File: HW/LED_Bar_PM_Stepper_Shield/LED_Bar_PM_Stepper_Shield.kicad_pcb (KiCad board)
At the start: 2 copper layers, 165.1 x 55.9 mm, 24 parts, among them J1 JST XH 5pin male socket, J2 JST XH 5pin male socket, J3 JST XH 5pin male socket, J4 JST XH 5pin male socket, J5 1x6 2.54mm female, pin2 filled, J6 1x6 2.54mm female, pin2 filled, J7 Extension of Ard Nano, filled, J8 Extension of Ard Nano, filled, U1 ULN2803A, U2 ULN2803A

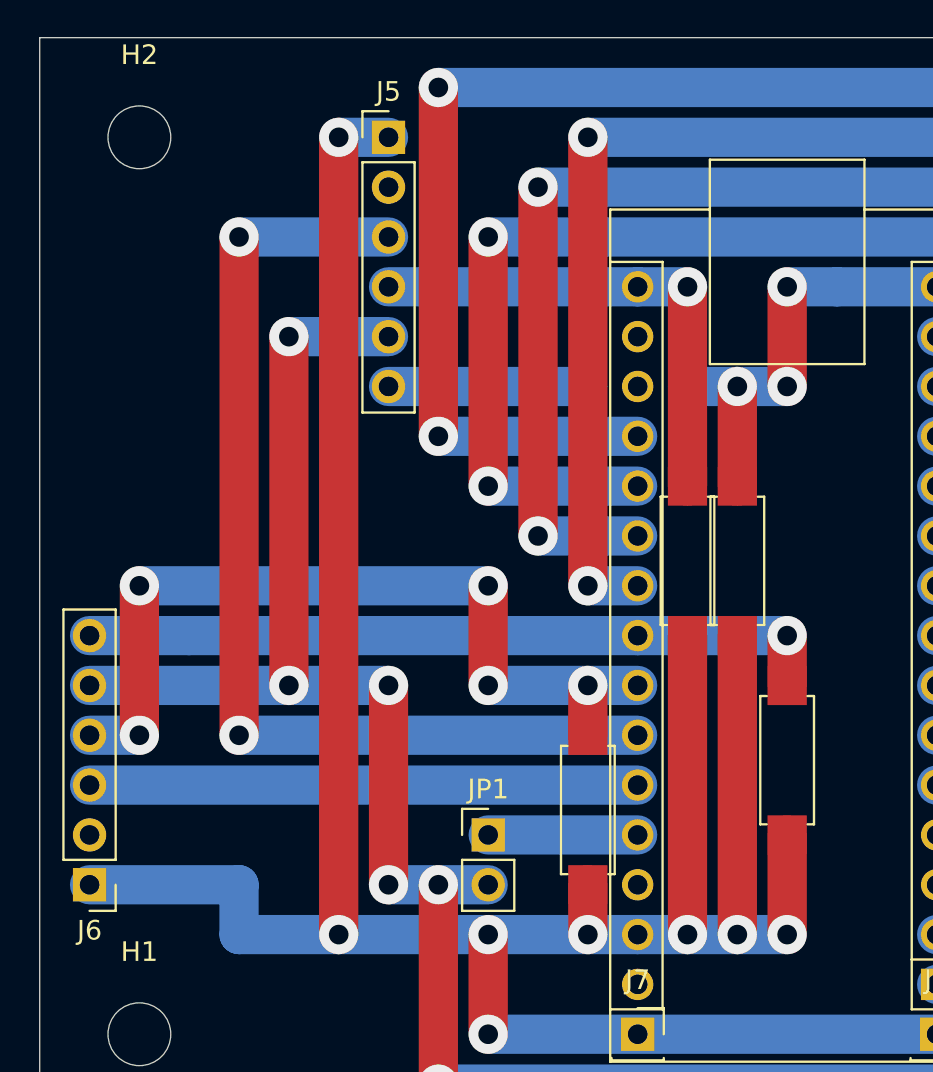
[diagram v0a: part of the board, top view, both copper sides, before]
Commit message: Swapped GND and 5V so I can use internal Pull-up.
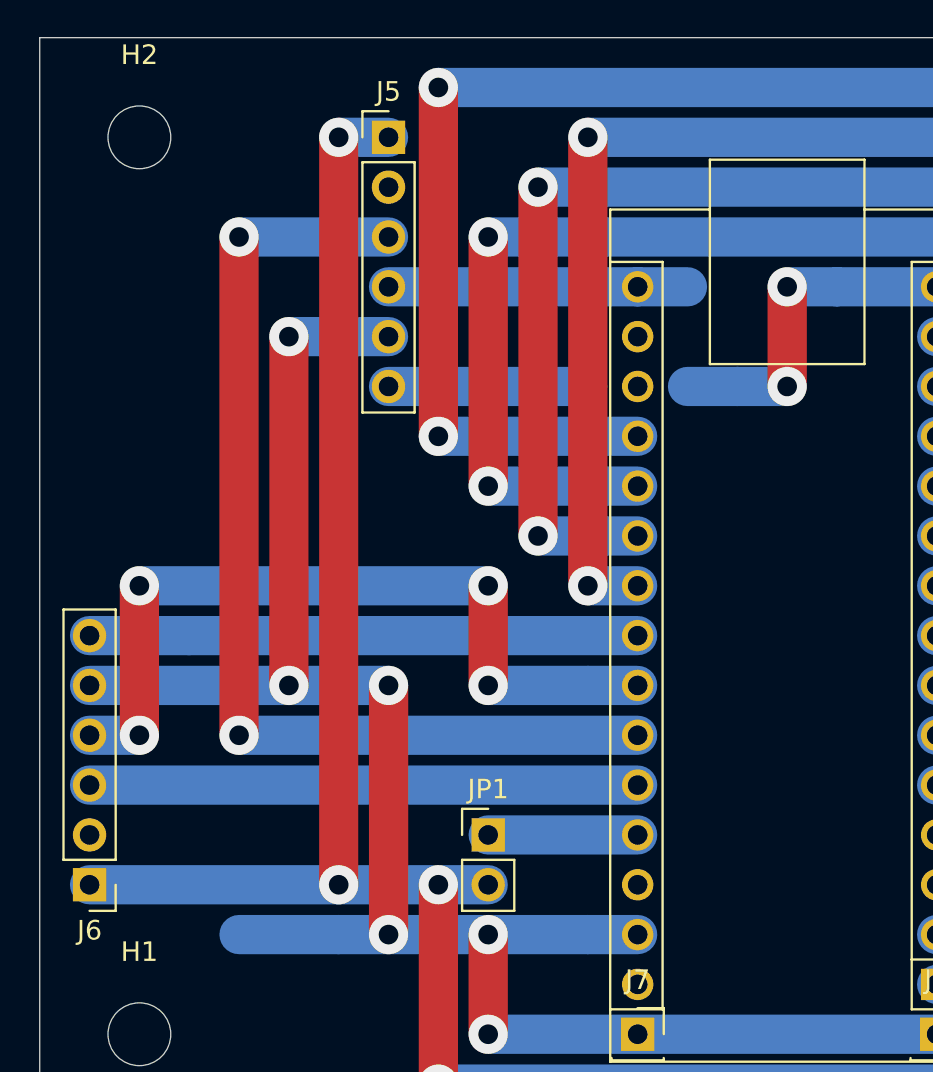
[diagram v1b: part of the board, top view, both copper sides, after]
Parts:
- removed R1, R2, R3, R4: 10k, For_Rasterboard:R_Axial_DIN0207_L6.3mm_D2.5mm_Pinf_Horizontal
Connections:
- J5 pad 1: GND -> +5V
- J5 pad 5: +5V -> GND
- J6 pad 1: GND -> +5V
- J6 pad 5: +5V -> GND
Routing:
- net GND: track 246.4 -> 198.1 mm, vias 12 -> 10
- net /DB1: track 38.1 -> 27.9 mm, vias 1 -> 0
- net /DA0: track 25.4 -> 15.2 mm, vias 1 -> 0
- net +5V: track 295.0 -> 302.6 mm, vias 14 -> 12
- net /DB0: track 33.0 -> 27.9 mm, vias 3 -> 2
- net /DA1: track 43.2 -> 40.6 mm, vias 5 -> 4

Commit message: All done.
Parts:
- added D3: 1N5400, Diode_THT:D_DO-201AD_P5.08mm_Vertical_AnodeUp, F.Cu at (215.9, 121.9)
- added D4: 3mm yellow, For_Rasterboard:LED_D3.0mm_Pinf, F.Cu at (198.1, 119.4)
- added D5: 1N5400, Diode_THT:D_DO-201AD_P5.08mm_Vertical_AnodeUp, F.Cu at (223.5, 124.5)
- added J10: 2-pin KK254, Connector_Molex:Molex_KK-254_AE-6410-02A_1x02_P2.54mm_Vertical, F.Cu at (193.0, 124.5)
- added J9: Barrel_Jack_Switch, Connector_BarrelJack:BarrelJack_Horizontal, F.Cu at (231.1, 123.5)
- added Q1: IRLZ34N, Package_TO_SOT_THT:TO-220-3_Vertical, F.Cu at (208.3, 124.5)
- added R1: 470, For_Rasterboard:R_Axial_DIN0207_L6.3mm_D2.5mm_P7.62mm_Horizontal, F.Cu at (203.2, 119.4)
- moved H1 5.08 mm to (86.4, 134.6)
- moved H3 5.08 mm to (241.3, 134.6)
- moved D2 2.54 mm to (223.5, 83.8)
- moved J3 2.54 mm to (205.7, 94.0)
- moved D1 2.54 mm to (172.7, 104.1)
- moved J1 2.54 mm to (154.9, 114.3)
- moved J2 2.54 mm to (165.1, 111.8)
- moved J4 2.54 mm to (215.9, 91.4)
- moved U1 2.54 mm to (139.7, 104.1)
- moved U2 2.54 mm to (190.5, 83.8)
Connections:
- net /b0/B2 renamed /S2
- net /b0/B3 renamed /S3
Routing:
- net /S3: track 10.2 -> 121.9 mm, vias 0 -> 4
- net GND: track 198.1 -> 236.6 mm
- net +5V: track 302.6 -> 329.8 mm, vias 12 -> 13
- net Net-(D3-A): track 0.00 -> 22.9 mm
- net Net-(D4-K): track 0.00 -> 5.08 mm, vias 0 -> 1
- net Net-(RN1-R6): track 5.08 -> 2.54 mm
- net Net-(RN2-R8): track 5.08 -> 2.54 mm
- net Net-(RN2-R7): track 5.08 -> 2.54 mm
- net Net-(RN2-R6): track 5.08 -> 2.54 mm
- net Net-(RN2-R5): track 5.08 -> 2.54 mm
- net Net-(RN2-R4): track 5.08 -> 2.54 mm
- net Net-(RN2-R3): track 5.08 -> 2.54 mm
- net Net-(RN2-R2): track 5.08 -> 2.54 mm
- net Net-(RN2-R1): track 5.08 -> 2.54 mm
- net Net-(RN1-R8): track 5.08 -> 2.54 mm
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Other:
- board size 165.1 x 55.9 mm -> 165.1 x 61 mm
